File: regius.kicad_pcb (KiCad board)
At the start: 2 copper layers, 65.1 x 56.1 mm, 23 parts, among them J1 Conn_01x02, J16 Conn_01x04, J7 Conn_01x02, J9 Conn_01x02, SW1 Reset, U3 samd51p20, U5 LM1117-3.3

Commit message: debug port
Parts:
- removed J1: Conn_01x02, Connector_PinHeader_2.54mm:PinHeader_1x02_P2.54mm_Vertical
- moved H4 144.3 mm to (106.3, 39.0), turned to 180 degrees
- moved C10 127.2 mm to (113.0, 46.3), turned to 90 degrees
- moved H6 120.5 mm to (106.3, 62.0), turned to 180 degrees
- moved U5 119.8 mm to (112.2, 54.6)
- moved J7 119.7 mm to (105.5, 55.8), turned to 180 degrees
- moved C9 119.5 mm to (107.5, 46.3), turned to 90 degrees
- moved C8 118.5 mm to (282.4, 94.1)
- moved H3 111.9 mm to (106.3, 88.0), turned to 180 degrees
- moved H5 91.4 mm to (164.3, 39.0), turned to 180 degrees
- moved U3 62.6 mm to (135.7, 71.6)
- moved SW1 59.3 mm to (152.9, 48.1)
- moved H1 45.5 mm to (164.3, 62.0), turned to 180 degrees
- moved R3 42.3 mm to (296.4, 117.6)
- moved J16 42.3 mm to (279.2, 82.6)
- moved J9 42.3 mm to (273.2, 74.6)
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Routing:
- removed copper zone on B.Cu, net GND
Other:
- board size 65.1 x 56.1 mm -> 65.1 x 82.2 mm

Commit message: add 3d image
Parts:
- removed C8: C0.1uf, Capacitor_SMD:C_0603_1608Metric
- removed J16: Conn_01x04, Connector_PinHeader_2.54mm:PinHeader_1x04_P2.54mm_Vertical
- removed R1, R11, R18, R2: 75, Resistor_SMD:R_0603_1608Metric
- removed R19, R3: 100, Resistor_SMD:R_0603_1608Metric
- removed R6: R10K, Resistor_SMD:R_0603_1608Metric
- moved J9 117.1 mm to (157.9, 94.7)
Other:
- board size 65.1 x 82.2 mm -> 65.1 x 84.8 mm

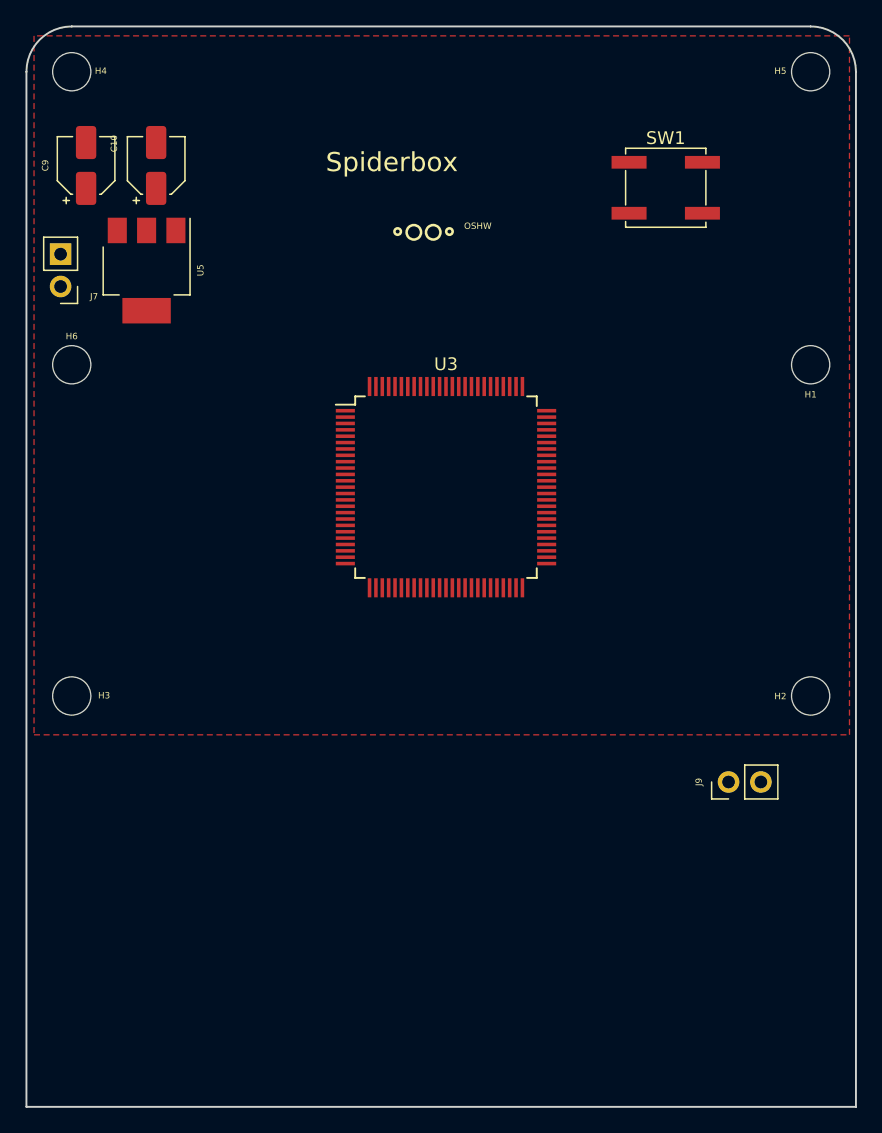
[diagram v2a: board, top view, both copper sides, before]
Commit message: update schematic tca9548
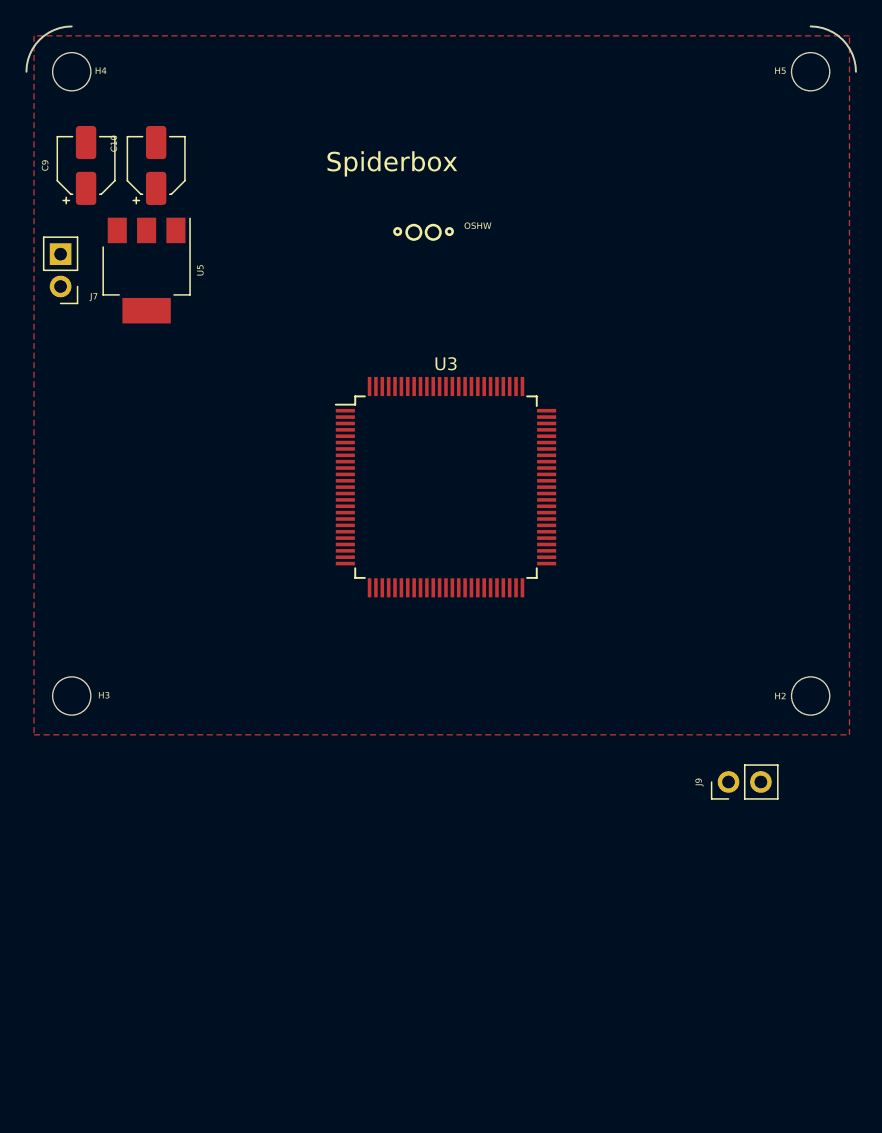
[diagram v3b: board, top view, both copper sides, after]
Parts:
- removed H1, H6: MountingHole, MountingHole:MountingHole_3mm
- removed SW1: Reset, Button_Switch_SMD:SW_SPST_EVPBF
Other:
- board size 65.1 x 84.8 mm -> 65.1 x 3.6 mm

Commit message: update layout design
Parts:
- added C1: C_Small, Capacitor_SMD:C_0603_1608Metric, F.Cu at (162.9, 147.3)
- added C11: C_Small, Capacitor_SMD:C_0603_1608Metric, F.Cu at (132.3, 74.4)
- added C12: C_Small, Capacitor_SMD:C_0603_1608Metric, F.Cu at (103.9, 71.3)
- added C13: C_Small, Capacitor_SMD:C_0603_1608Metric, F.Cu at (134.7, 50.8)
- added C14: C_Small, Capacitor_SMD:C_0603_1608Metric, F.Cu at (144.6, 52.7)
- added C15: C_Small, Capacitor_SMD:C_0603_1608Metric, F.Cu at (139.7, 50.8)
- added C16: C_Small, Capacitor_SMD:C_0603_1608Metric, F.Cu at (135.9, 74.4)
- added C17: C_Small, Capacitor_SMD:C_0603_1608Metric, F.Cu at (147.1, 70.9)
- added C18: C_Small, Capacitor_SMD:C_0603_1608Metric, F.Cu at (105.4, 63.3)
- added C19: C_Small, Capacitor_SMD:C_0603_1608Metric, F.Cu at (104.7, 58.5)
- added C2: C_Small, Capacitor_SMD:C_0603_1608Metric, F.Cu at (153.1, 136.1)
- added C20: C_Small, Capacitor_SMD:C_0603_1608Metric, F.Cu at (152.9, 143.3)
- added C21: C_Small, Capacitor_SMD:C_0603_1608Metric, F.Cu at (153.6, 140.6)
- added C3: C_Small, Capacitor_SMD:C_0603_1608Metric, F.Cu at (126.4, 68.5)
- added C4: C_Small, Capacitor_SMD:C_0603_1608Metric, F.Cu at (124.4, 62.0)
- added C5: C_Small, Capacitor_SMD:C_0603_1608Metric, F.Cu at (124.4, 59.0)
- added C6: C_Small, Capacitor_SMD:C_0603_1608Metric, F.Cu at (136.6, 51.2)
- added C7: C_Small, Capacitor_SMD:C_0603_1608Metric, F.Cu at (136.6, 47.9)
- added C8: C0.1uf, Capacitor_SMD:C_0603_1608Metric, F.Cu at (136.9, 41.3)
- added D1: LED_Small, LED_SMD:LED_0603_1608Metric, F.Cu at (148.0, 120.0)
- added D2: LED_Small, LED_SMD:LED_0603_1608Metric, F.Cu at (152.5, 118.2)
- added D3: LED_Small, LED_SMD:LED_0603_1608Metric, F.Cu at (192.7, 130.6)
- added D4: WS2812B, LED_SMD:LED_WS2812B_PLCC4_5.0x5.0mm_P3.2mm, F.Cu at (138.2, 29.0)
- added D5: WS2812B, LED_SMD:LED_WS2812B_PLCC4_5.0x5.0mm_P3.2mm, F.Cu at (146.2, 29.0)
- added D6: LED_Small, LED_SMD:LED_0603_1608Metric, F.Cu at (137.2, 147.1)
- added J1: 3.3v, Connector_PinHeader_2.54mm:PinHeader_1x02_P2.54mm_Vertical, F.Cu at (135.4, 116.8)
- added J10: A10, Connector_PinHeader_2.54mm:PinHeader_1x02_P2.54mm_Vertical, F.Cu at (120.4, 72.1)
- added J11: A9, Connector_PinHeader_2.54mm:PinHeader_1x02_P2.54mm_Vertical, F.Cu at (113.6, 70.3)
- added J12: A8, Connector_PinHeader_2.54mm:PinHeader_1x02_P2.54mm_Vertical, F.Cu at (120.4, 67.8)
- added J13: A7, Connector_PinHeader_2.54mm:PinHeader_1x02_P2.54mm_Vertical, F.Cu at (113.6, 66.1)
- added J14: A6, Connector_PinHeader_2.54mm:PinHeader_1x02_P2.54mm_Vertical, F.Cu at (120.4, 63.6)
- added J15: A5, Connector_PinHeader_2.54mm:PinHeader_1x02_P2.54mm_Vertical, F.Cu at (113.6, 61.8)
- added J16: A4, Connector_PinHeader_2.54mm:PinHeader_1x02_P2.54mm_Vertical, F.Cu at (120.4, 59.3)
- added J17: A3, Connector_PinHeader_2.54mm:PinHeader_1x02_P2.54mm_Vertical, F.Cu at (113.6, 57.6)
- added J18: A2, Connector_PinHeader_2.54mm:PinHeader_1x02_P2.54mm_Vertical, F.Cu at (120.4, 55.1)
- added J2: D3, Connector_PinHeader_2.54mm:PinHeader_1x02_P2.54mm_Vertical, F.Cu at (151.9, 69.6)
- added J20: D27, Connector_PinHeader_2.54mm:PinHeader_1x02_P2.54mm_Vertical, F.Cu at (139.9, 101.0)
- added J21: D26, Connector_PinHeader_2.54mm:PinHeader_1x02_P2.54mm_Vertical, F.Cu at (135.6, 100.6)
- added J24: D23, Connector_PinHeader_2.54mm:PinHeader_1x02_P2.54mm_Vertical, F.Cu at (144.4, 100.8)
- added J25: D22, Connector_PinHeader_2.54mm:PinHeader_1x02_P2.54mm_Vertical, F.Cu at (124.9, 93.3)
- added J26: D12, Connector_PinHeader_2.54mm:PinHeader_1x02_P2.54mm_Vertical, F.Cu at (151.9, 56.8)
- added J27: D11, Connector_PinHeader_2.54mm:PinHeader_1x02_P2.54mm_Vertical, F.Cu at (158.6, 56.8)
- added J28: D10, Connector_PinHeader_2.54mm:PinHeader_1x02_P2.54mm_Vertical, F.Cu at (165.4, 56.8)
- added J29: D9, Connector_PinHeader_2.54mm:PinHeader_1x02_P2.54mm_Vertical, F.Cu at (151.9, 61.1)
- added J3: D2, Connector_PinHeader_2.54mm:PinHeader_1x02_P2.54mm_Vertical, F.Cu at (158.6, 69.6)
- added J30: D8, Connector_PinHeader_2.54mm:PinHeader_1x02_P2.54mm_Vertical, F.Cu at (158.6, 61.1)
- added J31: D7, Connector_PinHeader_2.54mm:PinHeader_1x02_P2.54mm_Vertical, F.Cu at (165.4, 61.1)
- added J32: D6, Connector_PinHeader_2.54mm:PinHeader_1x02_P2.54mm_Vertical, F.Cu at (151.9, 65.3)
- added J33: D5, Connector_PinHeader_2.54mm:PinHeader_1x02_P2.54mm_Vertical, F.Cu at (158.6, 65.3)
- added J34: D4, Connector_PinHeader_2.54mm:PinHeader_1x02_P2.54mm_Vertical, F.Cu at (165.4, 65.3)
- added J35: D44, Connector_PinHeader_2.54mm:PinHeader_1x02_P2.54mm_Vertical, F.Cu at (124.9, 100.3)
- added J36: D43, Connector_PinHeader_2.54mm:PinHeader_1x02_P2.54mm_Vertical, F.Cu at (139.9, 93.8)
- added J37: D42, Connector_PinHeader_2.54mm:PinHeader_1x02_P2.54mm_Vertical, F.Cu at (143.9, 93.8)
- added J38: D41, Connector_PinHeader_2.54mm:PinHeader_1x02_P2.54mm_Vertical, F.Cu at (129.4, 100.1)
- added J39: D40, Connector_PinHeader_2.54mm:PinHeader_1x02_P2.54mm_Vertical, F.Cu at (135.9, 93.6)
- added J4: A15, Connector_PinHeader_2.54mm:PinHeader_1x02_P2.54mm_Vertical, F.Cu at (113.6, 83.1)
- added J40: CAN, Connector_PinHeader_2.54mm:PinHeader_1x03_P2.54mm_Vertical, F.Cu at (135.9, 78.2)
- added J41: I2C, Connector_PinHeader_2.54mm:PinHeader_1x02_P2.54mm_Vertical, F.Cu at (161.9, 83.1)
- added J42: D37, Connector_PinHeader_2.54mm:PinHeader_1x02_P2.54mm_Vertical, F.Cu at (161.9, 100.8)
- added J43: D36, Connector_PinHeader_2.54mm:PinHeader_1x02_P2.54mm_Vertical, F.Cu at (165.9, 94.1)
- added J44: D35, Connector_PinHeader_2.54mm:PinHeader_1x02_P2.54mm_Vertical, F.Cu at (157.9, 100.8)
- added J45: D34, Connector_PinHeader_2.54mm:PinHeader_1x02_P2.54mm_Vertical, F.Cu at (161.9, 94.1)
- added J46: D33, Connector_PinHeader_2.54mm:PinHeader_1x02_P2.54mm_Vertical, F.Cu at (149.9, 100.8)
- added J47: D32, Connector_PinHeader_2.54mm:PinHeader_1x02_P2.54mm_Vertical, F.Cu at (153.9, 100.8)
- added J48: D31, Connector_PinHeader_2.54mm:PinHeader_1x02_P2.54mm_Vertical, F.Cu at (149.9, 94.1)
- added J49: D30, Connector_PinHeader_2.54mm:PinHeader_1x02_P2.54mm_Vertical, F.Cu at (153.9, 94.1)
- added J5: A14, Connector_PinHeader_2.54mm:PinHeader_1x02_P2.54mm_Vertical, F.Cu at (120.4, 80.6)
- added J50: D29, Connector_PinHeader_2.54mm:PinHeader_1x02_P2.54mm_Vertical, F.Cu at (157.9, 94.1)
- added J57: D52, Connector_PinHeader_2.54mm:PinHeader_1x02_P2.54mm_Vertical, F.Cu at (129.1, 118.6)
- added J58: D50, Connector_PinHeader_2.54mm:PinHeader_1x02_P2.54mm_Vertical, F.Cu at (124.1, 118.6)
- added J59: D49, Connector_PinHeader_2.54mm:PinHeader_1x02_P2.54mm_Vertical, F.Cu at (116.1, 100.1)
- added J6: A13, Connector_PinHeader_2.54mm:PinHeader_1x02_P2.54mm_Vertical, F.Cu at (113.6, 78.8)
- added J60: D48, Connector_PinHeader_2.54mm:PinHeader_1x02_P2.54mm_Vertical, F.Cu at (116.1, 93.3)
- added J61: D47, Connector_PinHeader_2.54mm:PinHeader_1x02_P2.54mm_Vertical, F.Cu at (111.6, 100.1)
- added J62: D46, Connector_PinHeader_2.54mm:PinHeader_1x02_P2.54mm_Vertical, F.Cu at (111.6, 93.3)
- added J63: D45, Connector_PinHeader_2.54mm:PinHeader_1x02_P2.54mm_Vertical, F.Cu at (129.1, 93.3)
- added J64: DAC, Connector_PinHeader_2.54mm:PinHeader_1x02_P2.54mm_Vertical, F.Cu at (113.6, 50.8)
- added J65: AREF, Connector_PinHeader_2.54mm:PinHeader_1x02_P2.54mm_Vertical, F.Cu at (126.4, 44.5)
- added J66: DAC, Connector_PinHeader_2.54mm:PinHeader_1x02_P2.54mm_Vertical, F.Cu at (120.4, 50.8)
- added J67: Conn_02x05_Counter_Clockwise, Connector_PinHeader_1.27mm:PinHeader_2x05_P1.27mm_Vertical, F.Cu at (131.4, 40.7)
- added J68: TXRX1CAN, Connector_PinHeader_2.54mm:PinHeader_1x03_P2.54mm_Vertical, F.Cu at (131.4, 86.3)
- added J69: 4WIRELED, Connector_PinHeader_2.54mm:PinHeader_1x02_P2.54mm_Vertical, F.Cu at (130.4, 29.6)
- added J70: TXRX, Connector_PinHeader_2.54mm:PinHeader_1x03_P2.54mm_Vertical, F.Cu at (141.9, 45.8)
- added J71: Micro_SD_Card_Det, Connector_Card:microSD_HC_Hirose_DM3D-SF, F.Cu at (157.9, 33.3)
- added J72: I2C, Connector_PinHeader_2.54mm:PinHeader_1x02_P2.54mm_Vertical, F.Cu at (189.9, 59.8)
- added J73: I2C, Connector_PinHeader_2.54mm:PinHeader_1x02_P2.54mm_Vertical, F.Cu at (161.9, 79.1)
- added J74: USB_B_Micro, Connector_USB:USB_Micro-B_Amphenol_10103594-0001LF_Horizontal, F.Cu at (170.9, 49.6)
- added J75: I2C, Connector_PinHeader_2.54mm:PinHeader_1x02_P2.54mm_Vertical, F.Cu at (161.9, 75.1)
- added J76: I2C, Connector_PinHeader_2.54mm:PinHeader_1x02_P2.54mm_Vertical, F.Cu at (168.6, 87.1)
- added J77: I2C, Connector_PinHeader_2.54mm:PinHeader_1x02_P2.54mm_Vertical, F.Cu at (164.4, 87.1)
- added J78: I2C, Connector_PinHeader_2.54mm:PinHeader_1x02_P2.54mm_Vertical, F.Cu at (171.1, 83.1)
- added J79: I2C, Connector_PinHeader_2.54mm:PinHeader_1x02_P2.54mm_Vertical, F.Cu at (171.1, 79.1)
- added J8: A12, Connector_PinHeader_2.54mm:PinHeader_1x02_P2.54mm_Vertical, F.Cu at (120.4, 76.3)
- added J80: I2C, Connector_PinHeader_2.54mm:PinHeader_1x02_P2.54mm_Vertical, F.Cu at (168.6, 75.1)
- added JP1: SolderJumper_2_Open, Jumper:SolderJumper-2_P1.3mm_Open_RoundedPad1.0x1.5mm, F.Cu at (156.1, 77.1)
- added JP2: SolderJumper_2_Open, Jumper:SolderJumper-2_P1.3mm_Open_RoundedPad1.0x1.5mm, F.Cu at (152.4, 77.1)
- added JP3: SolderJumper_2_Open, Jumper:SolderJumper-2_P1.3mm_Open_RoundedPad1.0x1.5mm, F.Cu at (156.1, 74.3)
- added R1: R330, Resistor_SMD:R_0603_1608Metric, F.Cu at (137.9, 37.8)
- added R10: R10K, Resistor_SMD:R_0603_1608Metric, F.Cu at (169.3, 137.1)
- added R11: R10K, Resistor_SMD:R_0603_1608Metric, F.Cu at (181.8, 141.1)
- added R12: R10K, Resistor_SMD:R_0603_1608Metric, F.Cu at (173.6, 138.3)
- added R13: R1K, Resistor_SMD:R_0603_1608Metric, F.Cu at (178.4, 136.8)
- added R2: R1K, Resistor_SMD:R_0603_1608Metric, F.Cu at (145.1, 147.1)
- added R3: R1K, Resistor_SMD:R_0603_1608Metric, F.Cu at (173.4, 141.1)
- added R4: R1K, Resistor_SMD:R_0603_1608Metric, F.Cu at (160.4, 145.1)
- added R5: R1K, Resistor_SMD:R_0603_1608Metric, F.Cu at (157.4, 138.1)
- added R6: R10K, Resistor_SMD:R_0603_1608Metric, F.Cu at (135.9, 37.8)
- added R7: R10K, Resistor_SMD:R_0603_1608Metric, F.Cu at (177.7, 144.7)
- added R8: R10K, Resistor_SMD:R_0603_1608Metric, F.Cu at (147.2, 129.0)
- added R9: R10K, Resistor_SMD:R_0603_1608Metric, F.Cu at (163.4, 138.6)
- added SW1: Reset, Button_Switch_SMD:SW_SPST_EVPBF, F.Cu at (145.2, 36.5)
- added U1: GD25Q32CTIGR, GD25Q32CTIGR:SOIC127P600X175-8N, F.Cu at (126.7, 80.2)
- added U2: samd51p20, Package_QFP:TQFP-128_14x14mm_P0.4mm, F.Cu at (136.9, 63.0)
- added Y1: Crystal, Crystal:Crystal_SMD_3215-2Pin_3.2x1.5mm, F.Cu at (126.7, 54.8)
- J7: value Conn_01x02 -> VCC
- J9: value Conn_01x02 -> A11
- U3: value samd51p20 -> TCA9548APWR; footprint Package_QFP:LQFP-100_14x14mm_P0.5mm -> Package_SO:TSSOP-24_4.4x7.8mm_P0.65mm
- moved H2 55.6 mm to (216.9, 70.0)
- moved J9 48.6 mm to (113.6, 74.6), turned to 270 degrees
- moved H3 45.3 mm to (62.1, 98.1)
- moved H4 32.9 mm to (78.3, 21.7)
- moved J7 28.5 mm to (122.6, 33.1)
- moved H5 24.2 mm to (185.6, 27.5)
- moved U3 22.6 mm to (154.9, 83.5)
- moved C9 15.2 mm to (117.6, 35.1)
- moved U5 15.0 mm to (109.6, 39.8), turned to 180 degrees
- moved C10 6.15 mm to (117.6, 42.3), turned to 270 degrees
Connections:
- J9 pad 1: Net-(J9-Pad1) -> /A11
- J9 pad 2: Net-(J9-Pad2) -> GND
- U3 pad 12: Net-(U3-Pad12) -> GND
- U3 pad 24: Net-(U3-Pad24) -> +3V3
- U3 pad 3: Net-(U3-Pad3) -> /RESET
- U3 pad 5: (no net) -> Net-(J73-Pad1)
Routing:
- net +3V3: track 0.00 -> 40.6 mm, vias 0 -> 10
- net /RESET: track 0.00 -> 30.9 mm, vias 0 -> 1
- net /A15: track 0.00 -> 29.8 mm
- net Net-(D4-Pad4): track 0.00 -> 27.5 mm, vias 0 -> 2
- net /A13: track 0.00 -> 27.2 mm
- net /A11: track 0.00 -> 23.7 mm
- net /A14: track 0.00 -> 21.7 mm
- net /A9: track 0.00 -> 21.0 mm
- net /A12: track 0.00 -> 18.3 mm
- net /A5: track 0.00 -> 16.7 mm
- net /A3: track 0.00 -> 15.6 mm
- net /A10: track 0.00 -> 15.3 mm
- net /A2: track 0.00 -> 14.2 mm
- net Net-(J67-Pad8): track 0.00 -> 12.8 mm, vias 0 -> 1
- net Net-(R1-Pad1): track 0.00 -> 12.5 mm, vias 0 -> 2
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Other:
- board outline removed
- net class Default: clearance 0.2 -> 0.1
- net class power removed
- rule trace_clearance: 0.2 -> 0.1

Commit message: update layout
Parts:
- moved J1 82.5 mm to (169.6, 41.7), turned to 90 degrees
- moved J66 39.9 mm to (102.4, 86.4), turned to 0 degrees
- moved J65 10.6 mm to (116.4, 47.9)
- moved J7 7.71 mm to (114.9, 33.4)
- moved J64 3.38 mm to (111.9, 47.9), turned to 0 degrees
- moved C10 3.03 mm to (120.4, 41.2)
- moved C9 3.03 mm to (120.4, 33.9)
- moved J68 2.99 mm to (131.4, 83.3), turned to 180 degrees
- moved J70 2.95 mm to (141.1, 42.9)
- moved U5 2.56 mm to (112.2, 39.7)
- moved J77 2.53 mm to (161.9, 87.1), turned to 90 degrees
- moved C11 2.51 mm to (129.8, 74.7)
- moved J34 1.61 mm to (166.9, 64.9)
- moved J31 1.56 mm to (166.9, 60.9)
- moved J28 1.55 mm to (166.9, 56.8)
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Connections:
- net /usb_rx_+ renamed /+
- net /usb_tx_- renamed /-
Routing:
- net Net-(J71-Pad3): track 0.00 -> 29.0 mm, vias 0 -> 2
- net Net-(J71-Pad5): track 0.00 -> 25.8 mm, vias 0 -> 2
- net Net-(J71-Pad7): track 0.00 -> 24.6 mm
- net Net-(J71-Pad8): track 0.00 -> 24.4 mm
- net /D4: track 0.00 -> 23.7 mm
- net /D7: track 0.00 -> 23.1 mm
- net Net-(U1-Pad5): track 0.00 -> 20.3 mm, vias 0 -> 2
- net /A7: track 0.00 -> 18.4 mm, vias 0 -> 1
- net Net-(U1-Pad7): track 0.00 -> 18.4 mm, vias 0 -> 2
- net Net-(J80-Pad2): track 0.00 -> 18.3 mm
- net /D2: track 0.00 -> 17.1 mm
- net Net-(J79-Pad2): track 0.00 -> 17.1 mm
- net Net-(J78-Pad2): track 0.00 -> 16.0 mm
- net Net-(U1-Pad6): track 0.00 -> 15.9 mm
- net /D5: track 0.00 -> 15.8 mm
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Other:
- net class Default: trace_width 0.25 -> 0.18
- rule trace_min: 0.2 -> 0.1

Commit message: update layout
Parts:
- added J19: reset, Connector_PinHeader_2.54mm:PinHeader_1x02_P2.54mm_Vertical, F.Cu at (182.2, 118.9)
- added J22: D28, Connector_PinHeader_2.54mm:PinHeader_1x02_P2.54mm_Vertical, F.Cu at (147.2, 92.2)
- moved C1 102.8 mm to (126.6, 51.2), turned to 180 degrees
- moved C2 86.0 mm to (123.9, 55.2), turned to 90 degrees
- moved R11 74.0 mm to (151.6, 73.5), turned to 90 degrees
- moved R7 71.9 mm to (161.1, 74.8), turned to 180 degrees
- moved R12 67.9 mm to (153.3, 73.5), turned to 90 degrees
- moved R10 66.4 mm to (156.1, 72.0), turned to 180 degrees
- moved R8 57.9 mm to (161.1, 72.8), turned to 180 degrees
- moved J46 48.9 mm to (152.0, 52.0), turned to 90 degrees
- moved C18 47.3 mm to (97.4, 109.9)
- moved C12 44.5 mm to (101.9, 115.7)
- moved C19 43.7 mm to (98.3, 101.7)
- moved R9 42.8 mm to (174.6, 97.3)
- moved J50 42.1 mm to (159.5, 52.0), turned to 90 degrees
- moved J47 40.0 mm to (151.9, 60.9), turned to 90 degrees
- moved J48 38.4 mm to (159.4, 56.9), turned to 90 degrees
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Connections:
- R9 pad 2: /RESET -> Net-(J19-Pad1)
- U3 pad 3: /RESET -> Net-(J19-Pad1)
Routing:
- net /SDCD: track 0.00 -> 63.7 mm, vias 0 -> 2
- net Net-(J75-Pad2): track 0.00 -> 42.1 mm, vias 0 -> 1
- net /D23: track 0.00 -> 34.9 mm, vias 0 -> 1
- net /D44: track 0.00 -> 32.8 mm
- net Net-(J75-Pad1): track 0.00 -> 32.5 mm, vias 0 -> 1
- net /D40: track 0.00 -> 31.5 mm
- net Net-(R8-Pad2): track 0.00 -> 31.2 mm, vias 0 -> 2
- net /D26: track 0.00 -> 30.3 mm
- net /D42: track 0.00 -> 30.1 mm
- net /D22: track 0.00 -> 28.8 mm, vias 0 -> 1
- net Net-(R7-Pad2): track 0.00 -> 27.7 mm
- net /D28: track 0.00 -> 27.0 mm, vias 0 -> 1
- net Net-(J65-Pad1): track 0.00 -> 26.0 mm, vias 0 -> 1
- net /+: track 0.00 -> 25.8 mm
- net /-: track 0.00 -> 25.8 mm
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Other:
- net class Default: via_dia 0.6 -> 0.45; via_drill 0.4 -> 0.35
- rule via_min_drill: 0.3 -> 0.063
- rule via_min_size: 0.4 -> 0.127

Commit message: update layout
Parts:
- removed C21: C_Small, Capacitor_SMD:C_0603_1608Metric
- removed J57: D52, Connector_PinHeader_2.54mm:PinHeader_1x02_P2.54mm_Vertical
- removed J58: D50, Connector_PinHeader_2.54mm:PinHeader_1x02_P2.54mm_Vertical
- removed J69: 4WIRELED, Connector_PinHeader_2.54mm:PinHeader_1x02_P2.54mm_Vertical
- removed J72: I2C, Connector_PinHeader_2.54mm:PinHeader_1x02_P2.54mm_Vertical
- added J23: Conn_01x04, Connector_PinHeader_2.54mm:PinHeader_1x04_P2.54mm_Vertical, F.Cu at (144.8, 78.7)
- moved D3 116.7 mm to (132.4, 30.7), turned to 90 degrees
- moved R3 116.3 mm to (126.9, 34.5), turned to 90 degrees
- moved R13 115.2 mm to (115.0, 40.7)
- moved R4 114.8 mm to (129.7, 34.5), turned to 90 degrees
- moved R2 110.4 mm to (132.5, 37.4), turned to 180 degrees
- moved D6 109.6 mm to (110.6, 40.7), turned to 180 degrees
- moved R5 106.6 mm to (132.4, 34.5), turned to 90 degrees
- moved D1 91.8 mm to (126.9, 30.7), turned to 270 degrees
- moved D2 90.4 mm to (129.7, 30.7), turned to 90 degrees
- moved C20 79.3 mm to (148.5, 64.2), turned to 180 degrees
- moved C19 66.3 mm to (148.9, 58.8), turned to 180 degrees
- moved H2 57.0 mm to (170.5, 103.0)
- moved C18 53.7 mm to (139.2, 76.1), turned to 90 degrees
- moved C12 51.4 mm to (127.4, 71.2), turned to 90 degrees
- moved H3 45.1 mm to (107.0, 103.0)
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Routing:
- net /D47: track 0.00 -> 39.2 mm, vias 0 -> 1
- net +3V3: track 42.7 -> 79.6 mm, vias 11 -> 22
- net /D49: track 0.00 -> 36.7 mm, vias 0 -> 2
- net /D46: track 0.00 -> 32.7 mm, vias 0 -> 1
- net Net-(J19-Pad1): track 0.00 -> 30.6 mm
- net /D48: track 0.00 -> 29.9 mm, vias 0 -> 2
- net Net-(J23-Pad4): track 0.00 -> 22.9 mm, vias 0 -> 1
- net Net-(R5-Pad1): track 0.00 -> 22.6 mm
- net Net-(R3-Pad1): track 0.00 -> 21.9 mm, vias 0 -> 2
- net Net-(J76-Pad2): track 0.00 -> 21.9 mm
- net Net-(R4-Pad1): track 0.00 -> 21.1 mm
- net Net-(J76-Pad1): track 0.00 -> 19.4 mm, vias 0 -> 1
- net /D35: track 13.0 -> 32.3 mm, vias 0 -> 1
- net Net-(J23-Pad3): track 0.00 -> 18.1 mm, vias 0 -> 1
- net /D34: track 21.4 -> 37.9 mm
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- added copper zone on B.Cu, net +3V3
- added copper zone on F.Cu, net GND
- removed copper zone on F.Cu, net +3V3
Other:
- board outline added: 71 x 84 mm
